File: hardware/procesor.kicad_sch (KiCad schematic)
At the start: 14 parts

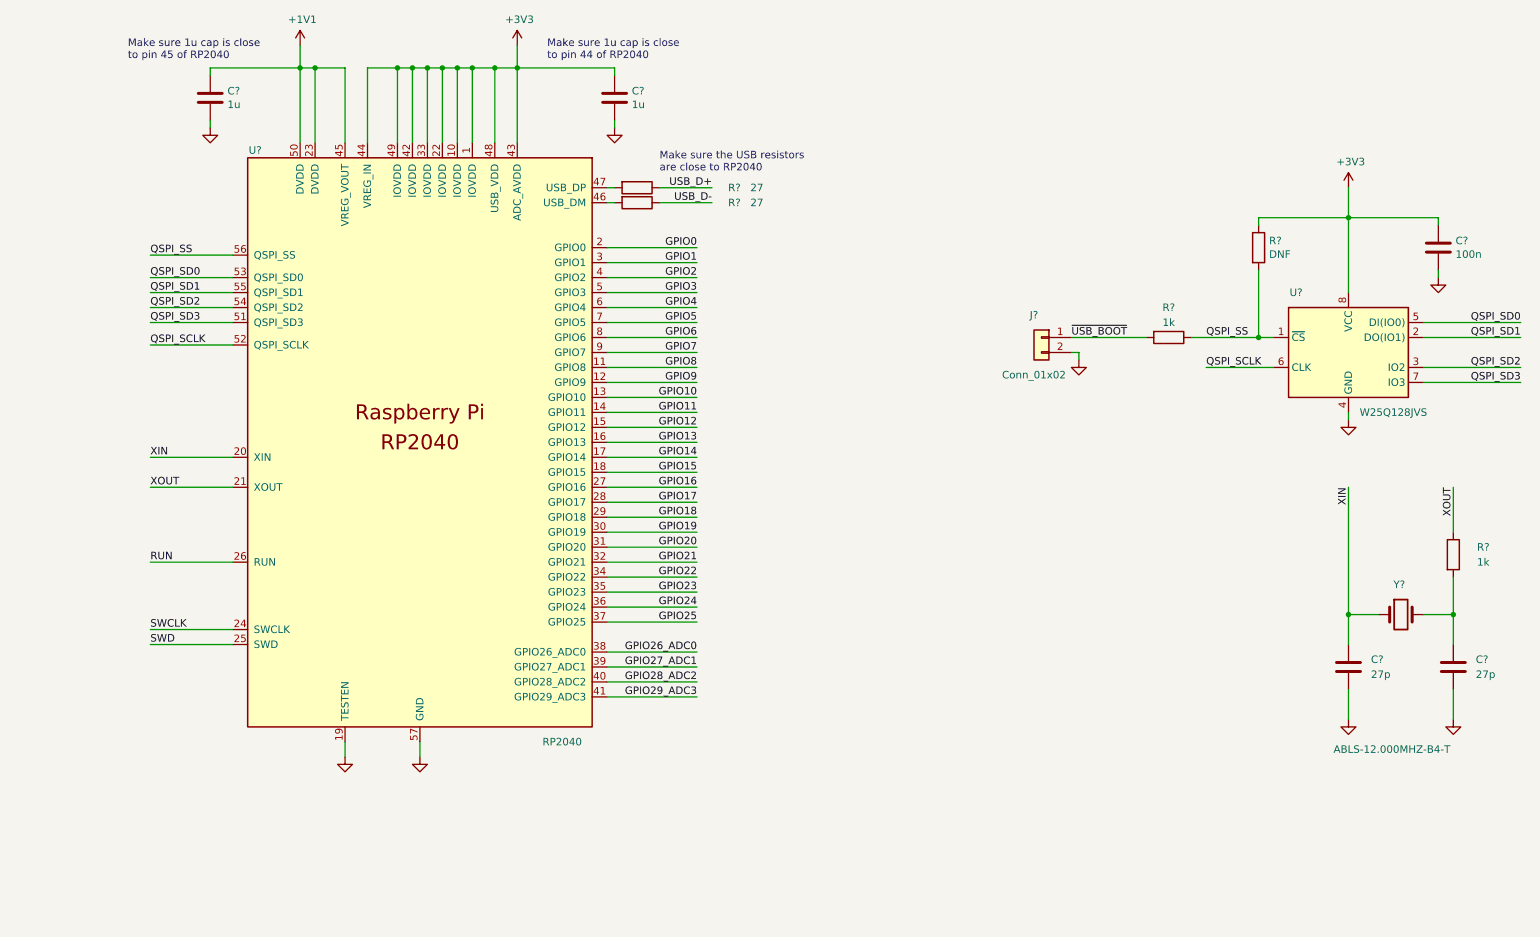
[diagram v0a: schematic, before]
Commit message: hw: Refactor Flash schem
- Add more technical look and feel to Flash schematic
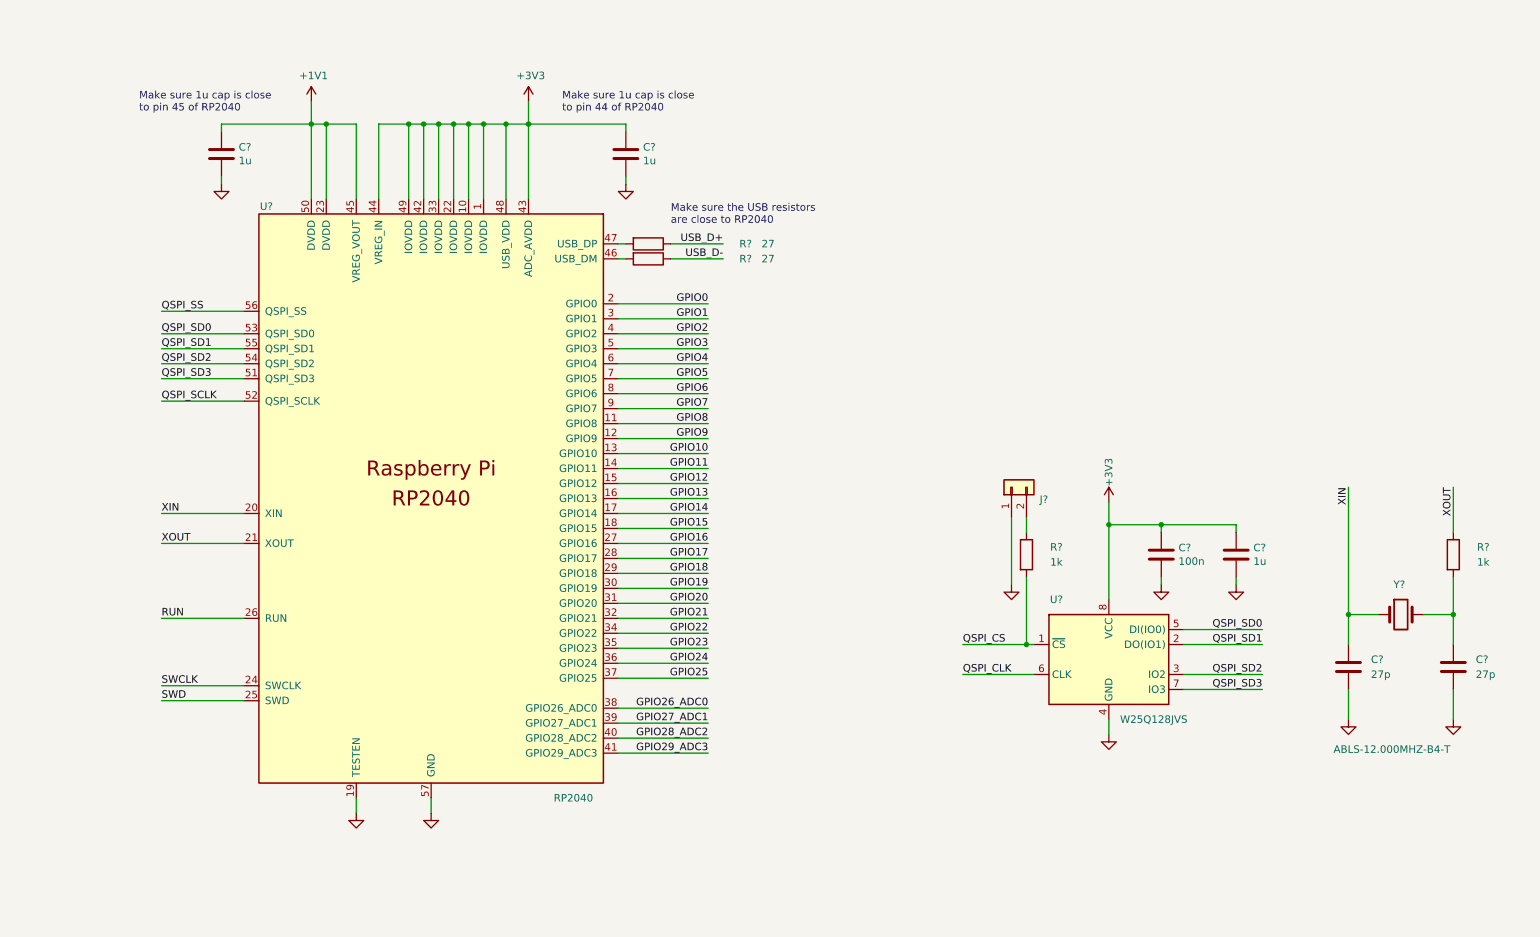
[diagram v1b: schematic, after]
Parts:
- removed C?: 100n, Capacitor_SMD:C_0603_1608Metric_Pad1.08x0.95mm_HandSolder, symbol Device:C
- removed J?: Conn_01x02, Connector_PinHeader_2.54mm:PinHeader_1x02_P2.54mm_Vertical, symbol Connector_Generic:Conn_01x02
- removed R?: 1k, Capacitor_SMD:C_0603_1608Metric_Pad1.08x0.95mm_HandSolder, symbol Device:R
- removed R?: DNF, Capacitor_SMD:C_0402_1005Metric, symbol Device:R
- removed U?: W25Q128JVS, Package_SO:SOIC-8_5.23x5.23mm_P1.27mm, symbol Memory_Flash:W25Q128JVS
- added C?: 1u, Capacitor_SMD:C_0603_1608Metric_Pad1.08x0.95mm_HandSolder, symbol Device:C
- added C?: 100n, Capacitor_SMD:C_0603_1608Metric_Pad1.08x0.95mm_HandSolder, symbol Device:C
- added J?: Conn_01x03, Connector_PinHeader_2.54mm:PinHeader_1x02_P2.54mm_Vertical, symbol Connector_Generic:Conn_01x02
- added R?: 1k, Capacitor_SMD:C_0603_1608Metric_Pad1.08x0.95mm_HandSolder, symbol Device:R
- added U?: W25Q128JVS, Package_SO:SOIC-8_5.23x5.23mm_P1.27mm, symbol Memory_Flash:W25Q128JVS
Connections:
- net +3V3: now also C?.1, C?.1, U?.8 (VCC)
- net GND: now also C?.2, C?.2, J?.1 (Pin_1), U?.4 (GND)
- net QSPI_SD0: now also U?.5 (DI(IO0))
- net QSPI_SD1: now also U?.2 (DO(IO1))
- net QSPI_SD2: now also U?.3 (IO2)
- net QSPI_SD3: now also U?.7 (IO3)
- new net: J?.2 (Pin_2), R?.1
- new net QSPI_CLK: U?.6 (CLK)
- new net QSPI_CS: R?.2, U?.1 (~{CS})
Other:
- moved on the sheet: C?, R?, U?

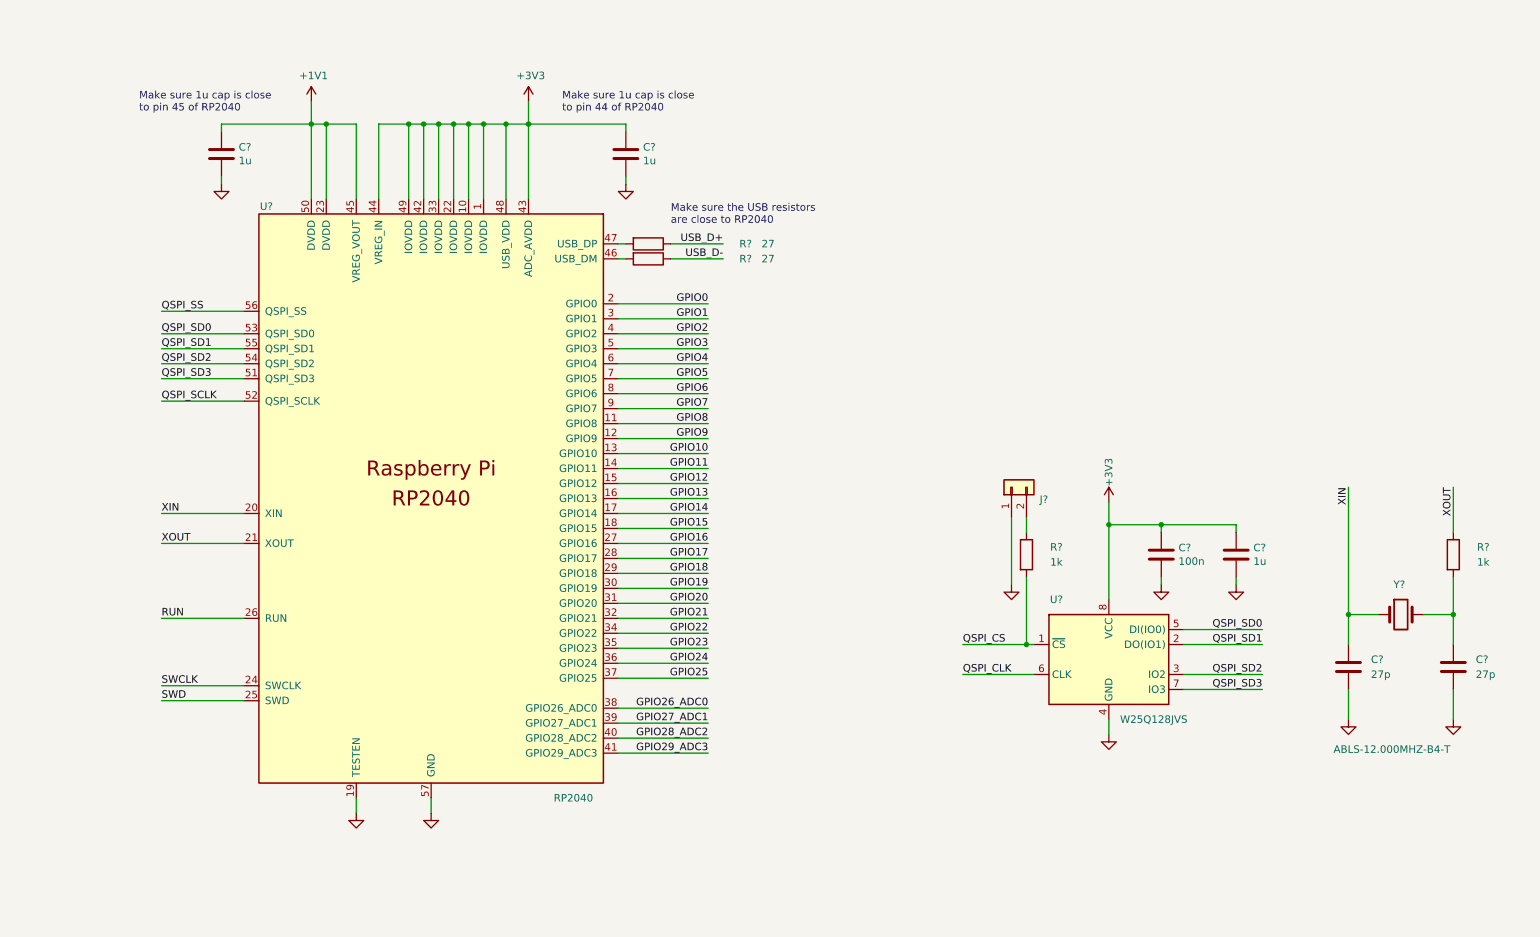
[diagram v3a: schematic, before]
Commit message: hw: Add CPU interface
- Add USB and debug interface
- Adjust schematic look
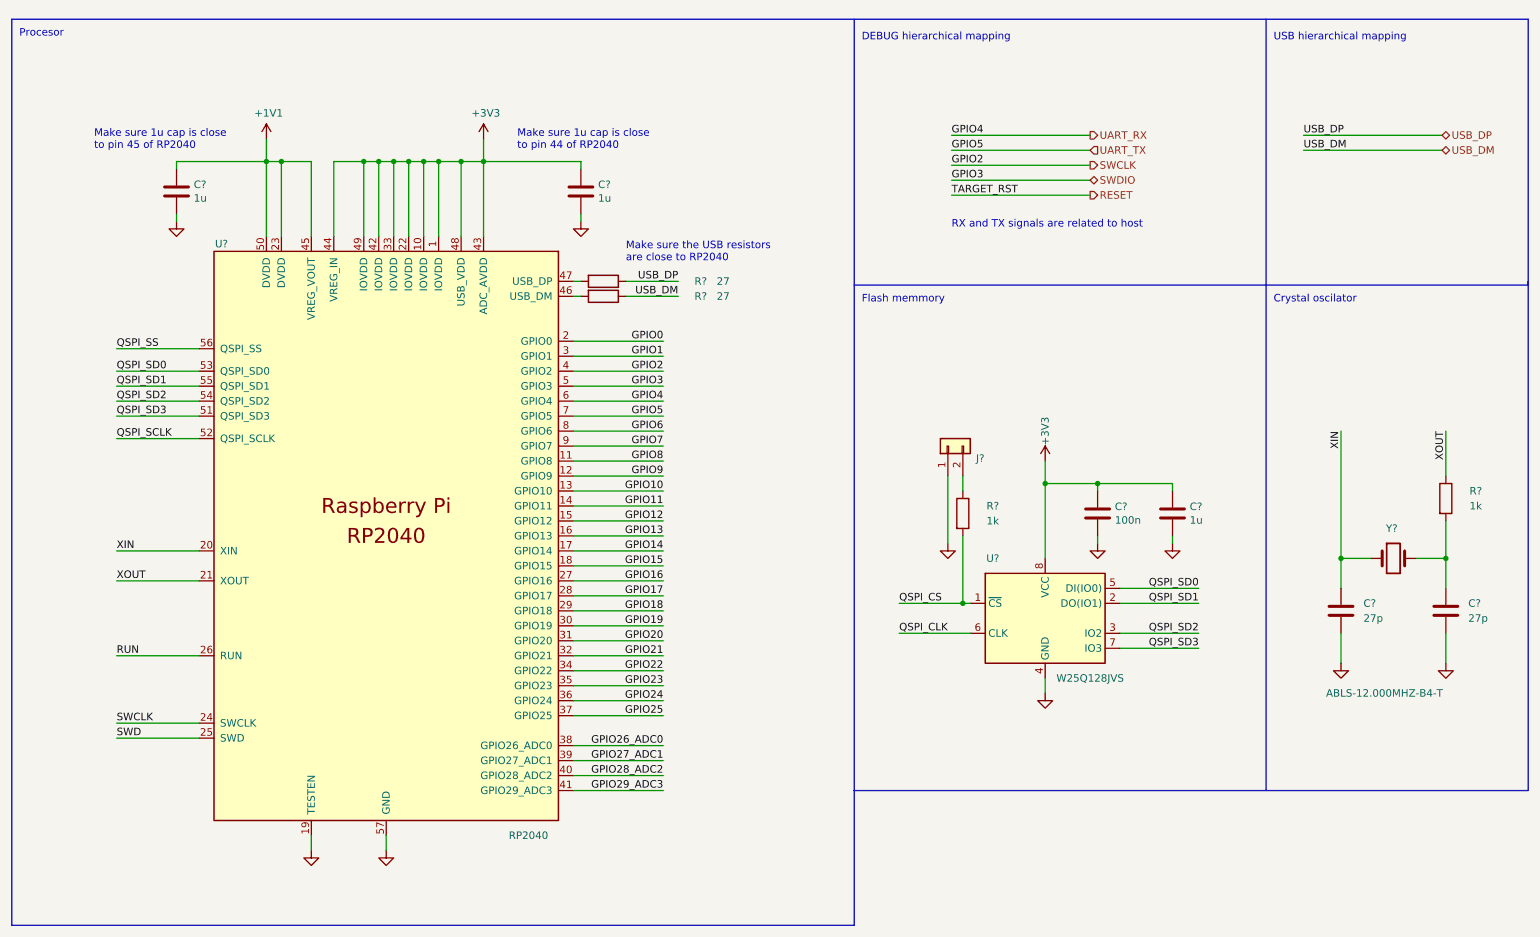
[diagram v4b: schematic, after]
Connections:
- net GPIO2 is gone; now on net SWCLK: U?.4 (GPIO2)
- net GPIO3 renamed SWDIO
- net GPIO4 renamed UART_RX
- net GPIO5 renamed UART_TX
- net USB_D+ renamed USB_DP
- net USB_D- renamed USB_DM
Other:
- note added: "Crystal oscilator"
- note added: "DEBUG hierarchical mapping"
- note added: "Flash memmory"
- note added: "Procesor"
- note added: "RX and TX signals are related to host"
- note added: "USB hierarchical mapping"
- moved on the sheet: C?, J?, R?, U?, Y?

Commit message: hw: Remove unnecesary pins and signals
- Mark all NC pins
- Rename QSPI signals to match Flash and CPU
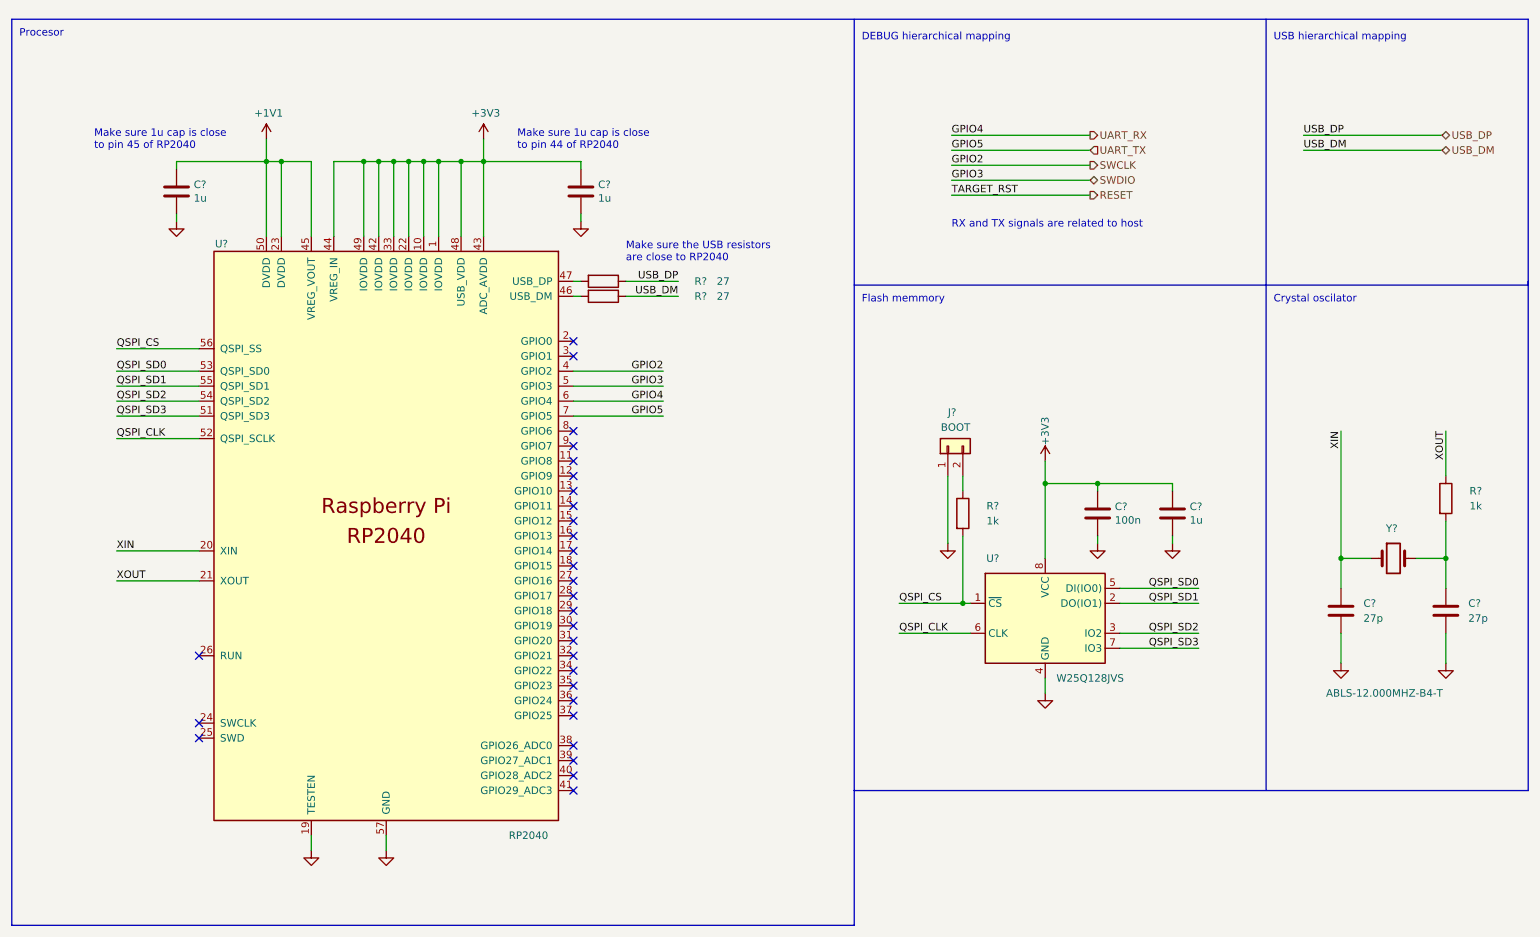
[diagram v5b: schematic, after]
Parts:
- J?: value Conn_01x03 -> BOOT
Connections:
- net QSPI_SCLK is gone; now on net QSPI_CLK: U?.52 (QSPI_SCLK)
- net QSPI_SS is gone; now on net QSPI_CS: U?.56 (QSPI_SS)
- net SWCLK: no longer U?.24 (SWCLK)
- net GPIO0: no longer names the net of U?.2 (GPIO0)
- net GPIO1: no longer names the net of U?.3 (GPIO1)
- net GPIO10: no longer names the net of U?.13 (GPIO10)
- net GPIO11: no longer names the net of U?.14 (GPIO11)
- net GPIO12: no longer names the net of U?.15 (GPIO12)
- net GPIO13: no longer names the net of U?.16 (GPIO13)
- net GPIO14: no longer names the net of U?.17 (GPIO14)
- net GPIO15: no longer names the net of U?.18 (GPIO15)
- net GPIO16: no longer names the net of U?.27 (GPIO16)
- net GPIO17: no longer names the net of U?.28 (GPIO17)
- net GPIO18: no longer names the net of U?.29 (GPIO18)
- net GPIO19: no longer names the net of U?.30 (GPIO19)
- net GPIO20: no longer names the net of U?.31 (GPIO20)
- net GPIO21: no longer names the net of U?.32 (GPIO21)
- net GPIO22: no longer names the net of U?.34 (GPIO22)
- net GPIO23: no longer names the net of U?.35 (GPIO23)
- net GPIO24: no longer names the net of U?.36 (GPIO24)
- net GPIO25: no longer names the net of U?.37 (GPIO25)
- net GPIO26_ADC0: no longer names the net of U?.38 (GPIO26_ADC0)
- net GPIO27_ADC1: no longer names the net of U?.39 (GPIO27_ADC1)
- net GPIO28_ADC2: no longer names the net of U?.40 (GPIO28_ADC2)
- net GPIO29_ADC3: no longer names the net of U?.41 (GPIO29_ADC3)
- net GPIO6: no longer names the net of U?.8 (GPIO6)
- net GPIO7: no longer names the net of U?.9 (GPIO7)
- net GPIO8: no longer names the net of U?.11 (GPIO8)
- net GPIO9: no longer names the net of U?.12 (GPIO9)
- net RUN: no longer names the net of U?.26 (RUN)
- net SWD: no longer names the net of U?.25 (SWD)
- no-connect marks 0 -> 29

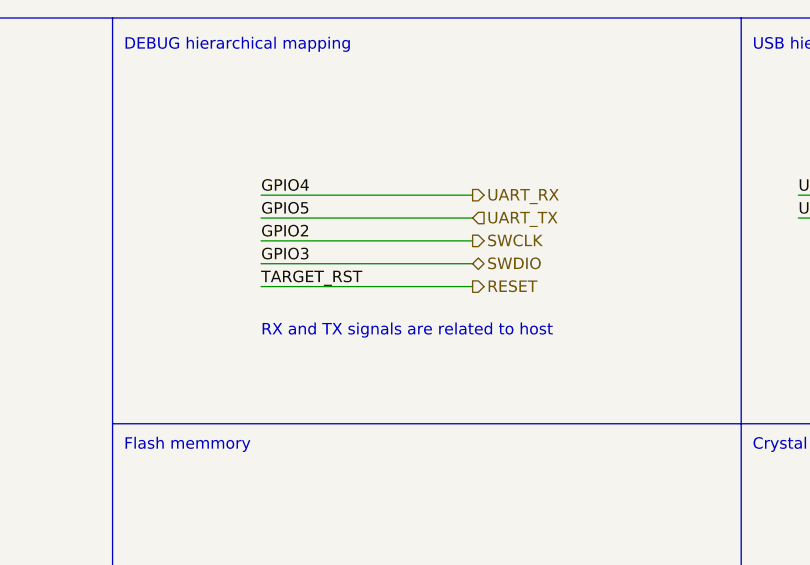
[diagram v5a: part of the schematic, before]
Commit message: hw: Add LEDs and reset buton to interface
- Remove interface signal from CPU
- Add LEDS for ON, RX, TX, DIO signals
- Add button tor target reset
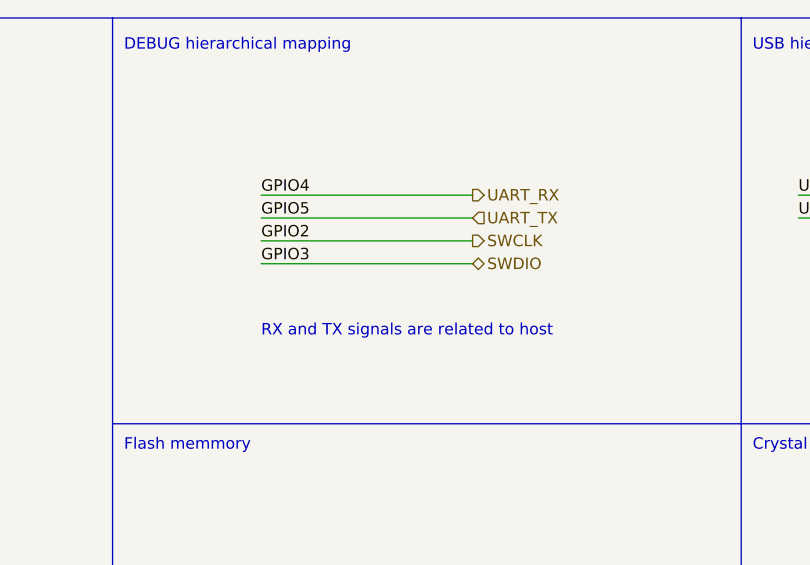
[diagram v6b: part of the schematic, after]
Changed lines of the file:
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@@
-    (stroke (width 0) (type default) (color 0 0 0 0))
-  )
-  (wire (pts (xy 179.07 59.69) (xy 202.565 59.69))
     (stroke (width 0) (type default) (color 0 0 0 0))
   )
@@
     (effects (font (size 1.27 1.27)) (justify left bottom))
   )
-  (label "TARGET_RST" (at 179.07 59.69 0)
-    (effects (font (size 1.27 1.27)) (justify left bottom))
-  )
   (label "USB_DP" (at 238.76 49.53 0)
     (effects (font (size 1.27 1.27)) (justify left bottom))
@@
     (effects (font (size 1.27 1.27)) (justify left))
   )
-  (hierarchical_label "RESET" (shape output) (at 202.565 59.69 0)
-    (effects (font (size 1.27 1.27)) (justify left))
-  )

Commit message: hw: Add the title block informations
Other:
- company: (none) -> Jan Krejčí
- title: (none) -> Pico probe
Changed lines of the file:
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@@
 (kicad_sch (version 20211123) (generator eeschema)
   (paper "A4")
+  (title_block
+    (title "Pico probe")
+    (date "2022-04-03")
+    (rev "22.04")
+    (company "Jan Krejčí")
+  )
   (junction (at 81.915 53.975) (diameter 0) (color 0 0 0 0)
   )
